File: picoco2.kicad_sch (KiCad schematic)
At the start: 19 parts, among them J1 Conn_01x03_Female, Q1 Q_NMOS_GDS, SW1 SW_Push, SW2 SW_Push, U1 PicoW, U2 scd30, U3 ssd1306

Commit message: update
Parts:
- removed D2: LED, LED_THT:LED_D5.0mm, symbol Device:LED
- added BT1: Battery, picoco2:CR1220-2, symbol Device:Battery
- added BT3: Battery, Connector_JST:JST_PH_S2B-PH-SM4-TB_1x02-1MP_P2.00mm_Horizontal, symbol Device:Battery
- added C1, C2, C3: C, Capacitor_SMD:C_0603_1608Metric_Pad1.08x0.95mm_HandSolder, symbol Device:C
- added D4: LED, LED_SMD:LED_0603_1608Metric_Pad1.05x0.95mm_HandSolder, symbol Device:LED
- added D5: D, Diode_SMD:D_SOD-123F, symbol Device:D
- added J2: Micro_SD_Card, picoco2:DM3D-SF_outline, symbol Connector:Micro_SD_Card
- added J3: Conn_01x03_Female, Connector_PinSocket_2.54mm:PinSocket_1x03_P2.54mm_Vertical, symbol Connector:Conn_01x03_Female
- added JP1: SolderJumper_2_Open, Jumper:SolderJumper-2_P1.3mm_Open_Pad1.0x1.5mm, symbol Jumper:SolderJumper_2_Open
- added R10, R11: R, Resistor_THT:R_Axial_DIN0204_L3.6mm_D1.6mm_P7.62mm_Horizontal, symbol Device:R
- added R5, R6, R9: R, Resistor_SMD:R_0603_1608Metric_Pad0.98x0.95mm_HandSolder, symbol Device:R
- added R7: 1K, Resistor_SMD:R_0603_1608Metric_Pad0.98x0.95mm_HandSolder, symbol Device:R
- added R8: 10K, Resistor_SMD:R_0603_1608Metric_Pad0.98x0.95mm_HandSolder, symbol Device:R
- added U4: PCF8523T, Package_SO:SOIC-8_3.9x4.9mm_P1.27mm, symbol Timer_RTC:PCF8523T
- added U5: MCP73831-2-OT, Package_TO_SOT_SMD:SOT-23-5, symbol Battery_Management:MCP73831-2-OT
- added Y1: Crystal_GND23, Crystal:Crystal_SMD_Abracon_ABS25-4Pin_8.0x3.8mm, symbol Device:Crystal_GND23
- BZ1: footprint Buzzer_Beeper:Buzzer_12x9.5RM7.6 -> Buzzer_Beeper:MagneticBuzzer_Kobitone_254-EMB84Q-RO
- D1: footprint Diode_THT:D_A-405_P7.62mm_Horizontal -> Diode_SMD:D_SOD-123F
- Q1: footprint Package_TO_SOT_THT:TO-220-3_Horizontal_TabDown -> Package_TO_SOT_SMD:SOT-23
- R1, R2, R3, R4: footprint Resistor_THT:R_Axial_DIN0207_L6.3mm_D2.5mm_P7.62mm_Horizontal -> Resistor_SMD:R_0603_1608Metric_Pad0.98x0.95mm_HandSolder
- U1: footprint RPi_Pico:RPi_PicoW_SMD_TH -> RPi_Pico:RPi_PicoW_SMD
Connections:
- net +3V3: now also C2.1, J2.4 (VDD), R10.1, R11.1, R5.1, R6.2, R9.1
- net GND: now also BZ1.2 (+), Q1.3 (S), R3.2, R4.2, SW1.2, SW2.2, BT1.2 (-), BT3.2 (-), C1.2, C2.2, C3.2, J2.6 (VSS), JP1.1 (A), R8.2, U4.4 (VSS), U5.2 (VSS); no longer U2.2 (GND)
- net VBAT_AAA: now reaches D1.2 (A)
- net VBAT_AAA: now also BT2.1 (+); no longer J1.1 (Pin_1)
- net at J1.2 (Pin_2): now also D1.1 (K); no longer BT2.1 (+)
- net at J1.3 (Pin_3): now also D5.1 (K)
- net SCD30_EN: now reaches Q1.1 (G)
- net SCD30_EN: now also R3.1
- net SCD30_GND: now reaches Q1.2 (D)
- net SCD30_GND: now also U2.2 (GND), JP1.2 (B)
- net SCL: now reaches R2.2, U2.4 (SDA), U3.4 (SDA)
- net SCL: now also U1.2 (GPIO1), U2.3 (SCL), U3.3 (SCL), U4.6 (SCL); no longer U1.26 (GPIO20)
- net SDA: now reaches U1.1 (GPIO0)
- net SDA: now also R1.2, U4.5 (SDA)
- net SCK: now reaches U1.14 (GPIO10)
- net SCK: now also J2.5 (CLK)
- net MOSI: now reaches U1.15 (GPIO11)
- net MOSI: now also J2.3 (CMD)
- net MISO: now reaches U1.16 (GPIO12)
- net MISO: now also J2.7 (DAT0)
- net VSYS: now reaches U1.39 (VSYS)
- net VSYS: now also J1.1 (Pin_1); no longer D1.1 (K)
- net SD_CS: now reaches U1.4 (GPIO2)
- net SD_CS: now also J2.2 (DAT3/CD)
- net VBUS: now reaches U1.40 (VBUS)
- net VBUS: now also D4.2 (A), U5.4 (VDD)
- net at R4.1: now also J3.2 (Pin_2)
- net BUT_A: now reaches SW1.1
- net BUT_A: now also R10.2, R5.2
- net BUT_B: now reaches SW2.1
- net BUT_B: now also R11.2, R9.2
- net BUZZER: now reaches BZ1.1 (-)
- new net: U4.2 (OSCO), Y1.1
- new net: U4.1 (OSCI), Y1.4
- new net: D4.1 (K), R7.1
- new net: R7.2, U5.1 (STAT)
- new net: BT1.1 (+), U4.3 (VBAT)
- new net: C1.1, R6.1, U4.8 (VDD)
- new net: R8.1, U5.5 (PROG)
- new net RTC_INT: U4.7 (~{INT1}/CLKOUT)
- new net VBAT_LIPO: BT3.1 (+), C3.1, D5.2 (A), U5.3 (VBAT)
- new net WRITE_EN: J3.3 (Pin_3)
- now unconnected: U1.27 (GPIO21)
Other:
- note added: "Li-on/po batt charger"
- note added: "co2 sensor"
- note added: "i2c pullups"
- note added: "ssd1306"
- note added: "write permit"
- moved on the sheet: BT2, BZ1, D1, H1, H2, H3, H4, J1, Q1, R1, R2, R3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

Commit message: basic layout done
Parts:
- added D2: D, Diode_THT:D_5W_P10.16mm_Horizontal, symbol Device:D
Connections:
- net VBAT_AAA: now also D2.2 (A)
- net at D1.1 (K), J1.2 (Pin_2): now also D2.1 (K)
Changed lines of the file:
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@@
   (junction (at 247.65 157.48) (diameter 0) (color 0 0 0 0)
   )
+  (junction (at 93.98 30.48) (diameter 0) (color 0 0 0 0)
+  )
   (junction (at 134.62 156.21) (diameter 0) (color 0 0 0 0)
   )
   (junction (at 83.82 144.78) (diameter 0) (color 0 0 0 0)
   )
+  (junction (at 106.68 30.48) (diameter 0) (color 0 0 0 0)
+  )
   (junction (at 134.62 177.8) (diameter 0) (color 0 0 0 0)
   )
+  (wire (pts (xy 93.98 30.48) (xy 96.52 30.48))
+    (stroke (width 0) (type default) (color 0 0 0 0))
+  )
   (wire (pts (xy 31.75 43.18) (xy 31.75 46.99))
     (stroke (width 0) (type default) (color 0 0 0 0))
@@
     (stroke (width 0) (type default) (color 0 0 0 0))
   )
+  (wire (pts (xy 106.68 30.48) (xy 116.84 30.48))
+    (stroke (width 0) (type default) (color 0 0 0 0))
+  )
   (wire (pts (xy 83.82 144.78) (xy 86.36 144.78))
     (stroke (width 0) (type default) (color 0 0 0 0))
   )
+  (wire (pts (xy 104.14 20.32) (xy 106.68 20.32))
+    (stroke (width 0) (type default) (color 0 0 0 0))
+  )
   (wire (pts (xy 27.94 111.76) (xy 27.94 118.11))
     (stroke (width 0) (type default) (color 0 0 0 0))
@@
     (stroke (width 0) (type default) (color 0 0 0 0))
   )
+  (wire (pts (xy 93.98 20.32) (xy 93.98 30.48))
+    (stroke (width 0) (type default) (color 0 0 0 0))
+  )
   (wire (pts (xy 34.29 187.96) (xy 45.72 187.96))
     (stroke (width 0) (type default) (color 0 0 0 0))
@@
     (stroke (width 0) (type default) (color 0 0 0 0))
   )
-  (wire (pts (xy 104.14 30.48) (xy 116.84 30.48))
+  (wire (pts (xy 104.14 30.48) (xy 106.68 30.48))
     (stroke (width 0) (type default) (color 0 0 0 0))
   )
@@
     (stroke (width 0) (type default) (color 0 0 0 0))
   )
+  (wire (pts (xy 106.68 20.32) (xy 106.68 30.48))
+    (stroke (width 0) (type default) (color 0 0 0 0))
+  )
   (wire (pts (xy 71.12 176.53) (xy 71.12 193.04))
     (stroke (width 0) (type default) (color 0 0 0 0))
@@
     (stroke (width 0) (type default) (color 0 0 0 0))
   )
-  (wire (pts (xy 80.01 30.48) (xy 96.52 30.48))
+  (wire (pts (xy 80.01 30.48) (xy 93.98 30.48))
     (stroke (width 0) (type default) (color 0 0 0 0))
   )
@@
   )
   (wire (pts (xy 161.29 140.97) (xy 161.29 135.89))
+    (stroke (width 0) (type default) (color 0 0 0 0))
+  )
+  (wire (pts (xy 96.52 20.32) (xy 93.98 20.32))
     (stroke (width 0) (type default) (color 0 0 0 0))
   )
@@
     (pin "8")
     (pin "9")
+  )
+  (symbol (lib_id "Device:D") (at 100.33 20.32 180) (unit 1)
+    (in_bom yes) (on_board yes) (fields_autoplaced)
+    (property "Reference" "D2" (id 0) (at 100.33 13.97 0))
+    (property "Value" "D" (id 1) (at 100.33 16.51 0))
+    (property "Footprint" "Diode_THT:D_5W_P10.16mm_Horizontal" (id 2) (at 100.33 20.32 0)
+      (effects (font (size 1.27 1.27)) hide)
+    )
+    (property "Datasheet" "~" (id 3) (at 100.33 20.32 0)
+      (effects (font (size 1.27 1.27)) hide)
+    )
+    (pin "1")
+    (pin "2")
   )
   (symbol (lib_id "Device:R") (at 125.73 78.74 90) (unit 1)
@@
       (reference "D1") (unit 1) (value "D") (footprint "Diode_SMD:D_SOD-123F")
     )
+    (path "/1e8b9c71-f3f5-4466-ab4e-3ff89e8858a6"
+      (reference "D2") (unit 1) (value "D") (footprint "Diode_THT:D_5W_P10.16mm_Horizontal")
+    )
     (path "/b01fb83a-2fdf-41b3-9ede-d615741b68b6"

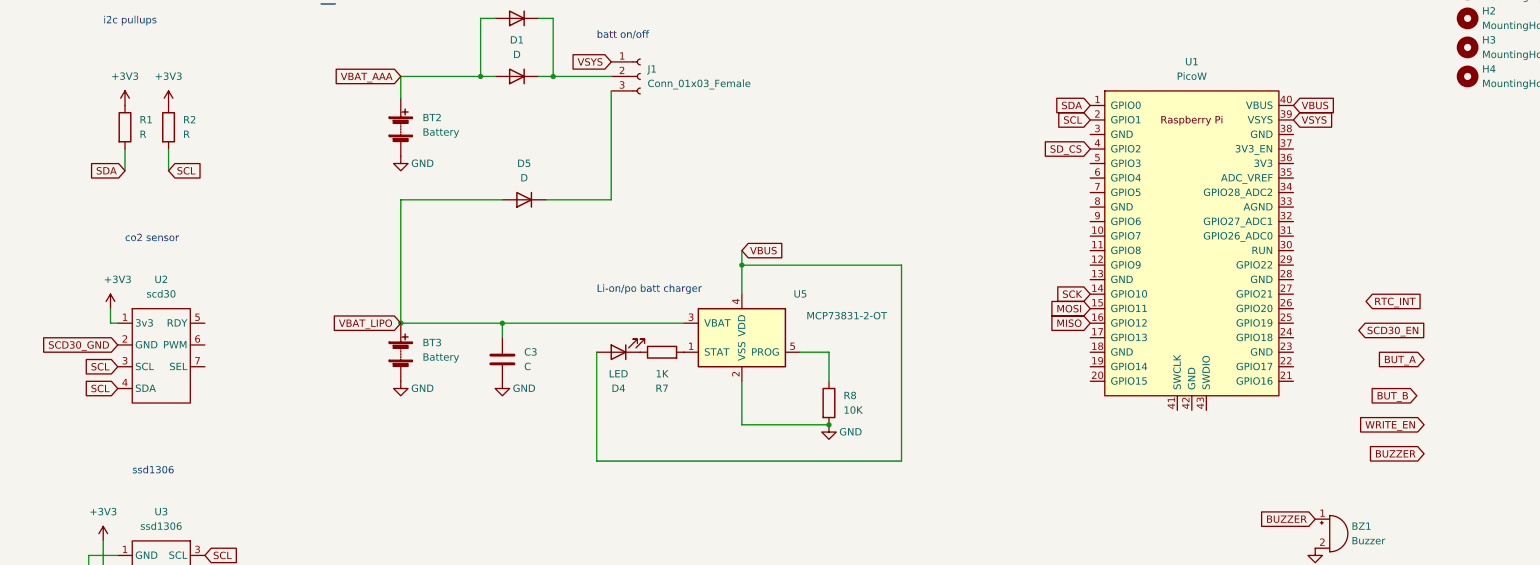
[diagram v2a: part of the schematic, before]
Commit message: added i2c resistors
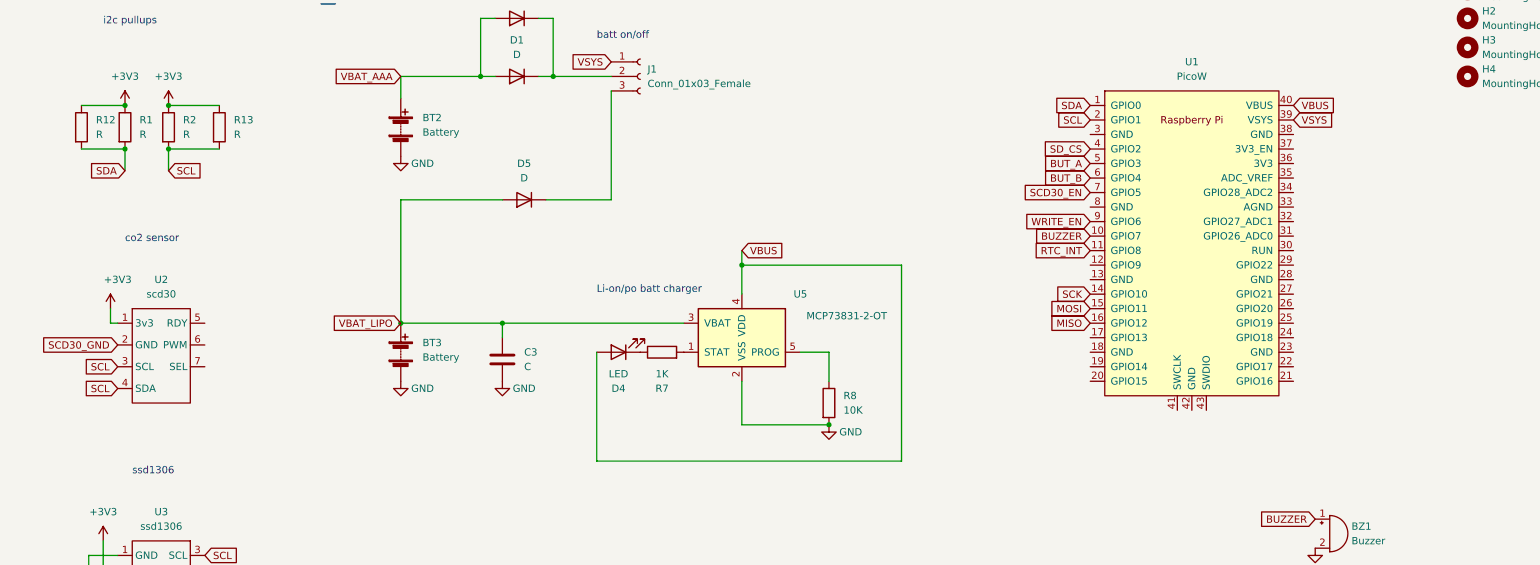
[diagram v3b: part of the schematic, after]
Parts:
- added R12, R13: R, Resistor_THT:R_Axial_DIN0204_L3.6mm_D1.6mm_P7.62mm_Horizontal, symbol Device:R
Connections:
- net +3V3: now also R12.1, R13.1
- net BUT_A: now also U1.5 (GPIO3)
- net BUT_B: now also U1.6 (GPIO4)
- net BUZZER: now also U1.10 (GPIO7)
- net RTC_INT: now also U1.11 (GPIO8)
- net SCD30_EN: now also U1.7 (GPIO5)
- net SCL: now also R13.2
- net SDA: now also R12.2
- net WRITE_EN: now also U1.9 (GPIO6)
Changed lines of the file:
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@@
   (junction (at 134.62 189.23) (diameter 0) (color 0 0 0 0)
   )
+  (junction (at 31.75 43.18) (diameter 0) (color 0 0 0 0)
+  )
+  (junction (at 39.37 35.56) (diameter 0) (color 0 0 0 0)
+  )
   (junction (at 62.23 144.78) (diameter 0) (color 0 0 0 0)
   )
@@
   (junction (at 134.62 162.56) (diameter 0) (color 0 0 0 0)
   )
+  (junction (at 31.75 35.56) (diameter 0) (color 0 0 0 0)
+  )
   (junction (at 80.01 73.66) (diameter 0) (color 0 0 0 0)
   )
@@
   (junction (at 134.62 156.21) (diameter 0) (color 0 0 0 0)
   )
+  (junction (at 39.37 43.18) (diameter 0) (color 0 0 0 0)
+  )
   (junction (at 83.82 144.78) (diameter 0) (color 0 0 0 0)
   )
@@
     (stroke (width 0) (type default) (color 0 0 0 0))
   )
+  (wire (pts (xy 39.37 43.18) (xy 48.26 43.18))
+    (stroke (width 0) (type default) (color 0 0 0 0))
+  )
   (wire (pts (xy 80.01 52.07) (xy 97.79 52.07))
     (stroke (width 0) (type default) (color 0 0 0 0))
@@
     (stroke (width 0) (type default) (color 0 0 0 0))
   )
+  (wire (pts (xy 24.13 43.18) (xy 31.75 43.18))
+    (stroke (width 0) (type default) (color 0 0 0 0))
+  )
   (wire (pts (xy 62.23 144.78) (xy 69.85 144.78))
+    (stroke (width 0) (type default) (color 0 0 0 0))
+  )
+  (wire (pts (xy 39.37 35.56) (xy 48.26 35.56))
+    (stroke (width 0) (type default) (color 0 0 0 0))
+  )
+  (wire (pts (xy 24.13 35.56) (xy 31.75 35.56))
     (stroke (width 0) (type default) (color 0 0 0 0))
   )
@@
     )
   )
-  (global_label "BUT_A" (shape input) (at 259.08 80.01 180) (fields_autoplaced)
-    (effects (font (size 1.27 1.27)) (justify right))
-    (property "Intersheet References" "${INTERSHEET_REFS}" (id 0) (at 251.0426 79.9306 0)
+  (global_label "BUT_A" (shape input) (at 200.66 45.72 180) (fields_autoplaced)
+    (effects (font (size 1.27 1.27)) (justify right))
+    (property "Intersheet References" "${INTERSHEET_REFS}" (id 0) (at 192.6226 45.6406 0)
       (effects (font (size 1.27 1.27)) (justify right) hide)
     )
@@
     )
   )
-  (global_label "BUT_B" (shape input) (at 257.81 86.36 180) (fields_autoplaced)
-    (effects (font (size 1.27 1.27)) (justify right))
-    (property "Intersheet References" "${INTERSHEET_REFS}" (id 0) (at 249.5912 86.2806 0)
+  (global_label "BUT_B" (shape input) (at 200.66 48.26 180) (fields_autoplaced)
+    (effects (font (size 1.27 1.27)) (justify right))
+    (property "Intersheet References" "${INTERSHEET_REFS}" (id 0) (at 192.4412 48.1806 0)
       (effects (font (size 1.27 1.27)) (justify right) hide)
     )
@@
     )
   )
-  (global_label "SCD30_EN" (shape input) (at 247.65 74.93 0) (fields_autoplaced)
-    (effects (font (size 1.27 1.27)) (justify left))
-    (property "Intersheet References" "${INTERSHEET_REFS}" (id 0) (at 259.6788 74.8506 0)
-      (effects (font (size 1.27 1.27)) (justify left) hide)
+  (global_label "SCD30_EN" (shape input) (at 200.66 50.8 180) (fields_autoplaced)
+    (effects (font (size 1.27 1.27)) (justify right))
+    (property "Intersheet References" "${INTERSHEET_REFS}" (id 0) (at 188.6312 50.8794 0)
+      (effects (font (size 1.27 1.27)) (justify right) hide)
     )
   )
@@
     )
   )
-  (global_label "WRITE_EN" (shape input) (at 259.08 91.44 180) (fields_autoplaced)
-    (effects (font (size 1.27 1.27)) (justify right))
-    (property "Intersheet References" "${INTERSHEET_REFS}" (id 0) (at 247.7769 91.3606 0)
-      (effects (font (size 1.27 1.27)) (justify right) hide)
-    )
-  )
-  (global_label "BUZZER" (shape input) (at 259.08 96.52 180) (fields_autoplaced)
-    (effects (font (size 1.27 1.27)) (justify right))
-    (property "Intersheet References" "${INTERSHEET_REFS}" (id 0) (at 249.2283 96.4406 0)
+  (global_label "WRITE_EN" (shape input) (at 200.66 55.88 180) (fields_autoplaced)
+    (effects (font (size 1.27 1.27)) (justify right))
+    (property "Intersheet References" "${INTERSHEET_REFS}" (id 0) (at 189.3569 55.8006 0)
+      (effects (font (size 1.27 1.27)) (justify right) hide)
+    )
+  )
+  (global_label "BUZZER" (shape input) (at 200.66 58.42 180) (fields_autoplaced)
+    (effects (font (size 1.27 1.27)) (justify right))
+    (property "Intersheet References" "${INTERSHEET_REFS}" (id 0) (at 190.8083 58.3406 0)
       (effects (font (size 1.27 1.27)) (justify right) hide)
     )
@@
     )
   )
-  (global_label "RTC_INT" (shape input) (at 248.92 69.85 0) (fields_autoplaced)
-    (effects (font (size 1.27 1.27)) (justify left))
-    (property "Intersheet References" "${INTERSHEET_REFS}" (id 0) (at 258.7112 69.7706 0)
-      (effects (font (size 1.27 1.27)) (justify left) hide)
+  (global_label "RTC_INT" (shape input) (at 200.66 60.96 180) (fields_autoplaced)
+    (effects (font (size 1.27 1.27)) (justify right))
+    (property "Intersheet References" "${INTERSHEET_REFS}" (id 0) (at 190.8688 61.0394 0)
+      (effects (font (size 1.27 1.27)) (justify right) hide)
     )
   )
@@
     (pin "2")
   )
+  (symbol (lib_id "Device:R") (at 24.13 39.37 0) (unit 1)
+    (in_bom yes) (on_board yes) (fields_autoplaced)
+    (property "Reference" "R12" (id 0) (at 26.67 38.0999 0)
+      (effects (font (size 1.27 1.27)) (justify left))
+    )
+    (property "Value" "R" (id 1) (at 26.67 40.6399 0)
+      (effects (font (size 1.27 1.27)) (justify left))
+    )
+    (property "Footprint" "Resistor_THT:R_Axial_DIN0204_L3.6mm_D1.6mm_P7.62mm_Horizontal" (id 2) (at 22.352 39.37 90)
+      (effects (font (size 1.27 1.27)) hide)
+    )
+    (property "Datasheet" "~" (id 3) (at 24.13 39.37 0)
+      (effects (font (size 1.27 1.27)) hide)
+    )
+    (pin "1")
+    (pin "2")
+  )
   (symbol (lib_id "Device:R") (at 31.75 39.37 0) (unit 1)
     (in_bom yes) (on_board yes) (fields_autoplaced)
@@
     )
     (property "Datasheet" "~" (id 3) (at 31.75 39.37 0)
+      (effects (font (size 1.27 1.27)) hide)
+    )
+    (pin "1")
+    (pin "2")
+  )
+  (symbol (lib_id "Device:R") (at 48.26 39.37 0) (unit 1)
+    (in_bom yes) (on_board yes) (fields_autoplaced)
+    (property "Reference" "R13" (id 0) (at 50.8 38.0999 0)
+      (effects (font (size 1.27 1.27)) (justify left))
+    )
+    (property "Value" "R" (id 1) (at 50.8 40.6399 0)
+      (effects (font (size 1.27 1.27)) (justify left))
+    )
+    (property "Footprint" "Resistor_THT:R_Axial_DIN0204_L3.6mm_D1.6mm_P7.62mm_Horizontal" (id 2) (at 46.482 39.37 90)
+      (effects (font (size 1.27 1.27)) hide)
+    )
+    (property "Datasheet" "~" (id 3) (at 48.26 39.37 0)
       (effects (font (size 1.27 1.27)) hide)
     )
@@
       (reference "R11") (unit 1) (value "R") (footprint "Resistor_THT:R_Axial_DIN0204_L3.6mm_D1.6mm_P7.62mm_Horizontal")
     )
+    (path "/4011fa0e-48f5-4fd9-9370-a57a889afe66"
+      (reference "R12") (unit 1) (value "R") (footprint "Resistor_THT:R_Axial_DIN0204_L3.6mm_D1.6mm_P7.62mm_Horizontal")
+    )
+    (path "/4c8c89b2-38a6-41c6-bd98-2803ad9fa73c"
+      (reference "R13") (unit 1) (value "R") (footprint "Resistor_THT:R_Axial_DIN0204_L3.6mm_D1.6mm_P7.62mm_Horizontal")
+    )
     (path "/d3fbd5d9-edde-42e2-941e-f1cb0af1d541"

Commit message: update
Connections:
- net SCL: no longer U2.4 (SDA)
- net SDA: now also U2.4 (SDA)
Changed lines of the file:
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@@
     )
   )
-  (global_label "SCL" (shape input) (at 30.48 85.09 180) (fields_autoplaced)
+  (global_label "SDA" (shape input) (at 30.48 85.09 180) (fields_autoplaced)
     (effects (font (size 1.27 1.27)) (justify right))
-    (property "Intersheet References" "${INTERSHEET_REFS}" (id 0) (at 24.5593 85.0106 0)
+    (property "Intersheet References" "${INTERSHEET_REFS}" (id 0) (at 24.4988 85.0106 0)
       (effects (font (size 1.27 1.27)) (justify right) hide)
     )
